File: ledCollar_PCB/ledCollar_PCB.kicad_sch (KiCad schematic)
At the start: 42 parts, among them J1 PWR+, J2 PWR-, J3 APA102, J6 SWD, Q1 AO3400A, Q2 Senba SMD0805-20, SW1 SW_Push, U1 AP2112K-3.3, U2 STM32F103C8Tx, U3 NRF24L01_Breakout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

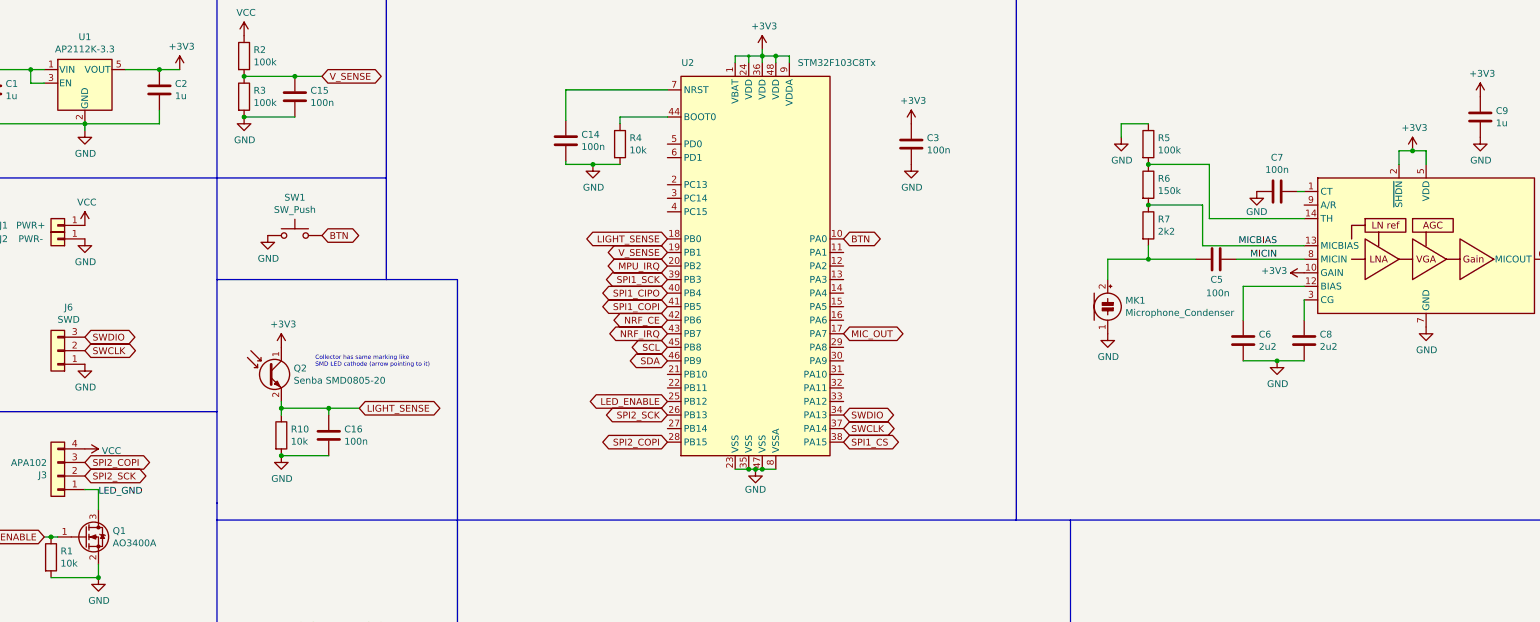
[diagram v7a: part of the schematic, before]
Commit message: fix quiescent current of MAX9814 and voltage dividers
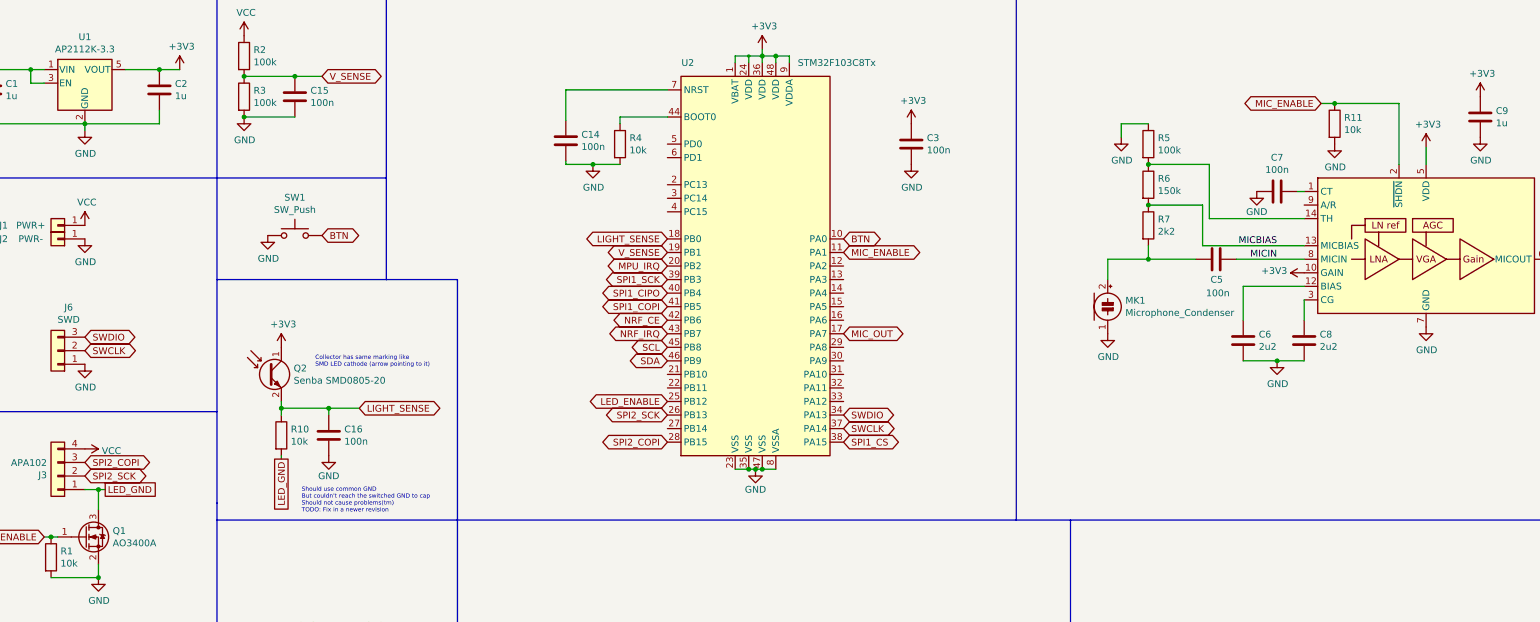
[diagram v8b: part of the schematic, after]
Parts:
- added R11: 10k, Resistor_SMD:R_0603_1608Metric, symbol Device:R
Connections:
- net +3V3: no longer U4.2 (~SHDN)
- net GND: now also R11.2; no longer R10.2
- net LED_GND: now also R10.2
- net MIC_ENABLE: now reaches U2.11 (PA1)
- net MIC_ENABLE: now also U4.2 (~SHDN), R11.1
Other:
- note added: "Should use common GND But couldn't reach the switched GND to cap Should not cause problems(tm) TODO: Fix in a newer revision"
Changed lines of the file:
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@@
   (junction (at 40.64 36.195) (diameter 0) (color 0 0 0 0))
   (junction (at 40.64 156.21) (diameter 0) (color 0 0 0 0))
+  (junction (at 43.18 104.775) (diameter 0) (color 0 0 0 0))
   (junction (at 43.18 121.285) (diameter 0) (color 0 0 0 0))
   (junction (at 44.45 143.51) (diameter 0) (color 0 0 0 0))
@@
   (junction (at 72.39 143.51) (diameter 0) (color 0 0 0 0))
   (junction (at 77.47 89.535) (diameter 0) (color 0 0 0 0))
-  (junction (at 77.47 98.425) (diameter 0) (color 0 0 0 0))
   (junction (at 80.01 27.305) (diameter 0) (color 0 0 0 0))
   (junction (at 86.36 89.535) (diameter 0) (color 0 0 0 0))
@@
   (junction (at 240.03 61.595) (diameter 0) (color 0 0 0 0))
   (junction (at 264.16 80.645) (diameter 0) (color 0 0 0 0))
-  (junction (at 289.56 41.275) (diameter 0) (color 0 0 0 0))
+  (junction (at 274.955 32.385) (diameter 0) (color 0 0 0 0))
   (wire (pts (xy 19.05 26.035) (xy 22.86 26.035))
     (stroke (width 0) (type solid) (color 0 0 0 0))
@@
     (stroke (width 0) (type solid) (color 0 0 0 0))
   )
+  (wire (pts (xy 43.18 104.775) (xy 44.45 104.775))
+    (stroke (width 0) (type solid) (color 0 0 0 0))
+  )
   (wire (pts (xy 43.18 118.745) (xy 43.18 121.285))
     (stroke (width 0) (type solid) (color 0 0 0 0))
@@
     (stroke (width 0) (type solid) (color 0 0 0 0))
   )
-  (wire (pts (xy 77.47 98.425) (xy 86.36 98.425))
+  (wire (pts (xy 77.47 98.425) (xy 77.47 99.06))
     (stroke (width 0) (type solid) (color 0 0 0 0))
   )
@@
     (stroke (width 0) (type solid) (color 0 0 0 0))
   )
-  (wire (pts (xy 287.02 41.275) (xy 289.56 41.275))
-    (stroke (width 0) (type solid) (color 0 0 0 0))
-  )
-  (wire (pts (xy 287.02 43.815) (xy 287.02 41.275))
-    (stroke (width 0) (type solid) (color 0 0 0 0))
-  )
-  (wire (pts (xy 292.1 41.275) (xy 289.56 41.275))
-    (stroke (width 0) (type solid) (color 0 0 0 0))
-  )
-  (wire (pts (xy 292.1 43.815) (xy 292.1 41.275))
+  (wire (pts (xy 272.415 32.385) (xy 274.955 32.385))
+    (stroke (width 0) (type solid) (color 0 0 0 0))
+  )
+  (wire (pts (xy 287.02 32.385) (xy 274.955 32.385))
+    (stroke (width 0) (type solid) (color 0 0 0 0))
+  )
+  (wire (pts (xy 287.02 43.815) (xy 287.02 32.385))
+    (stroke (width 0) (type solid) (color 0 0 0 0))
+  )
+  (wire (pts (xy 292.1 40.64) (xy 292.1 43.815))
     (stroke (width 0) (type solid) (color 0 0 0 0))
   )
@@
   (polyline (pts (xy 336.55 12.065) (xy 336.55 110.49))
     (stroke (width 0) (type solid) (color 0 0 0 0))
+  )
+  (text "Should use common GND\nBut couldn't reach the switched GND to cap\nShould not cause problems(tm)\nTODO: Fix in a newer revision"
+    (at 81.28 109.22 0)
+    (effects (font (size 0.8 0.8)) (justify left bottom))
   )
   (text "Collector has same marking like       \nSMD LED cathode (arrow pointing to it)"
@@
     (effects (font (size 1 1)) (justify left bottom))
   )
-  (label "LED_GND" (at 43.18 106.045 0)
-    (effects (font (size 1.27 1.27)) (justify left bottom))
-  )
   (label "MICBIAS" (at 264.16 59.055 180)
     (effects (font (size 1.27 1.27)) (justify right bottom))
@@
     (effects (font (size 1.27 1.27)) (justify left))
   )
+  (global_label "LED_GND" (shape passive) (at 44.45 104.775 0)
+    (effects (font (size 1.27 1.27)) (justify left))
+  )
+  (global_label "LED_GND" (shape passive) (at 77.47 99.06 270)
+    (effects (font (size 1.27 1.27)) (justify right))
+  )
   (global_label "V_SENSE" (shape bidirectional) (at 85.09 27.305 0)
     (effects (font (size 1.27 1.27)) (justify left))
@@
     (effects (font (size 1.27 1.27)) (justify left))
   )
+  (global_label "MIC_ENABLE" (shape bidirectional) (at 182.88 60.325 0)
+    (effects (font (size 1.27 1.27)) (justify left))
+  )
   (global_label "MIC_OUT" (shape bidirectional) (at 182.88 75.565 0)
     (effects (font (size 1.27 1.27)) (justify left))
@@
     (effects (font (size 1.27 1.27)) (justify right))
   )
+  (global_label "MIC_ENABLE" (shape bidirectional) (at 272.415 32.385 180)
+    (effects (font (size 1.27 1.27)) (justify right))
+  )
   (global_label "MIC_OUT" (shape bidirectional) (at 314.96 61.595 0)
     (effects (font (size 1.27 1.27)) (justify left))
@@
     )
   )
-  (symbol (lib_id "power:+3V3") (at 289.56 41.275 0)
-    (in_bom yes) (on_board yes)
-    (property "Reference" "#PWR0118" (id 0) (at 289.56 45.085 0)
-      (effects (font (size 1.27 1.27)) hide)
-    )
-    (property "Value" "+3V3" (id 1) (at 289.9283 36.9506 0))
-    (property "Footprint" "" (id 2) (at 289.56 41.275 0)
-      (effects (font (size 1.27 1.27)) hide)
-    )
-    (property "Datasheet" "" (id 3) (at 289.56 41.275 0)
+  (symbol (lib_id "power:+3V3") (at 292.1 40.64 0)
+    (in_bom yes) (on_board yes)
+    (property "Reference" "#PWR0118" (id 0) (at 292.1 44.45 0)
+      (effects (font (size 1.27 1.27)) hide)
+    )
+    (property "Value" "+3V3" (id 1) (at 292.4683 36.3156 0))
+    (property "Footprint" "" (id 2) (at 292.1 40.64 0)
+      (effects (font (size 1.27 1.27)) hide)
+    )
+    (property "Datasheet" "" (id 3) (at 292.1 40.64 0)
       (effects (font (size 1.27 1.27)) hide)
     )
@@
     )
   )
-  (symbol (lib_id "power:GND") (at 77.47 98.425 0)
-    (in_bom yes) (on_board yes)
-    (property "Reference" "#PWR0131" (id 0) (at 77.47 104.775 0)
-      (effects (font (size 1.27 1.27)) hide)
-    )
-    (property "Value" "GND" (id 1) (at 77.5843 102.7494 0))
-    (property "Footprint" "" (id 2) (at 77.47 98.425 0)
-      (effects (font (size 1.27 1.27)) hide)
-    )
-    (property "Datasheet" "" (id 3) (at 77.47 98.425 0)
-      (effects (font (size 1.27 1.27)) hide)
-    )
-  )
   (symbol (lib_id "power:GND") (at 81.28 142.24 0)
     (in_bom yes) (on_board yes)
@@
     )
   )
+  (symbol (lib_id "power:GND") (at 86.36 98.425 0) (unit 1)
+    (in_bom yes) (on_board yes)
+    (property "Reference" "#PWR0131" (id 0) (at 86.36 104.775 0)
+      (effects (font (size 1.27 1.27)) hide)
+    )
+    (property "Value" "GND" (id 1) (at 86.36 102.235 0))
+    (property "Footprint" "" (id 2) (at 86.36 98.425 0)
+      (effects (font (size 1.27 1.27)) hide)
+    )
+    (property "Datasheet" "" (id 3) (at 86.36 98.425 0)
+      (effects (font (size 1.27 1.27)) hide)
+    )
+  )
   (symbol (lib_id "power:GND") (at 93.98 142.24 0)
     (in_bom yes) (on_board yes)
@@
     )
   )
+  (symbol (lib_id "power:GND") (at 274.955 40.005 0)
+    (in_bom yes) (on_board yes)
+    (property "Reference" "#PWR0144" (id 0) (at 274.955 46.355 0)
+      (effects (font (size 1.27 1.27)) hide)
+    )
+    (property "Value" "GND" (id 1) (at 275.0693 44.3294 0))
+    (property "Footprint" "" (id 2) (at 274.955 40.005 0)
+      (effects (font (size 1.27 1.27)) hide)
+    )
+    (property "Datasheet" "" (id 3) (at 274.955 40.005 0)
+      (effects (font (size 1.27 1.27)) hide)
+    )
+  )
   (symbol (lib_id "power:GND") (at 292.1 74.295 0)
     (in_bom yes) (on_board yes)
@@
     )
     (property "Datasheet" "~" (id 3) (at 240.03 55.245 0)
+      (effects (font (size 1.27 1.27)) hide)
+    )
+  )
+  (symbol (lib_id "Device:R") (at 274.955 36.195 0)
+    (in_bom yes) (on_board yes)
+    (property "Reference" "R11" (id 0) (at 276.7331 35.0456 0)
+      (effects (font (size 1.27 1.27)) (justify left))
+    )
+    (property "Value" "10k" (id 1) (at 276.733 37.344 0)
+      (effects (font (size 1.27 1.27)) (justify left))
+    )
+    (property "Footprint" "Resistor_SMD:R_0603_1608Metric" (id 2) (at 273.177 36.195 90)
+      (effects (font (size 1.27 1.27)) hide)
+    )
+    (property "Datasheet" "~" (id 3) (at 274.955 36.195 0)
       (effects (font (size 1.27 1.27)) hide)
     )
@@
     )
   )
-  (symbol (lib_id "Device:C") (at 80.01 31.115 180) (unit 1)
+  (symbol (lib_id "Device:C") (at 80.01 31.115 180)
     (in_bom yes) (on_board yes)
     (property "Reference" "C15" (id 0) (at 82.9311 29.9656 0)
@@
     )
   )
-  (symbol (lib_id "Device:C") (at 86.36 94.615 180) (unit 1)
+  (symbol (lib_id "Device:C") (at 86.36 94.615 180)
     (in_bom yes) (on_board yes)
     (property "Reference" "C16" (id 0) (at 89.2811 93.4656 0)
@@
       (reference "#PWR0130") (unit 1)
     )
-    (path "/062168ac-497f-4e46-9272-b04306557664"
+    (path "/50124f71-2956-420d-8b6f-b373ef4dcd01"
       (reference "#PWR0131") (unit 1)
     )
@@
       (reference "#PWR0143") (unit 1)
     )
+    (path "/8ad78c1a-8add-4452-910c-9f0b046d0d4c"
+      (reference "#PWR0144") (unit 1)
+    )
     (path "/bbebd2f4-9685-40e0-9522-a5708083ab20"
       (reference "C1") (unit 1)
@@
       (reference "R10") (unit 1)
     )
+    (path "/5182b5e2-b612-4bd5-9d33-090fb510a125"
+      (reference "R11") (unit 1)
+    )
     (path "/a91595b9-50d8-4cbb-89e7-03d7bce19dcc"
